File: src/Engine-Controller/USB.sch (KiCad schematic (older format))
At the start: 1 part, among them P2 USB

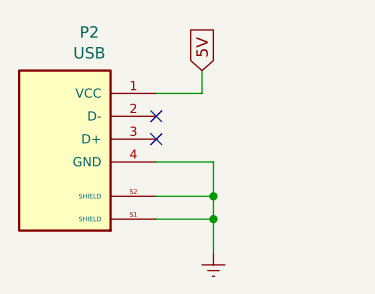
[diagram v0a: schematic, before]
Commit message: Wired 5V power multiplexor
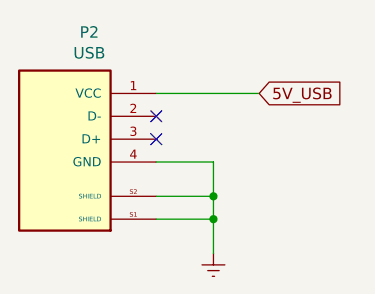
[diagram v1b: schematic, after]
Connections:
- net 5V renamed 5V_USB
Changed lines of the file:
@@
 Wire Wire Line
 	5950 4450 5950 4600
-Wire Wire Line
-	5700 3900 5900 3900
-Wire Wire Line
-	5900 3900 5900 3800
 $Comp
 L Engine-Controller:USB P2
@@
 	-1   0    0    -1
 $EndComp
-Text GLabel 5900 3800 1    50   Input ~ 0
-5V
+Text GLabel 6150 3900 2    50   Input ~ 0
+5V_USB
 NoConn ~ 5700 4000
 NoConn ~ 5700 4100
+Wire Wire Line
+	5700 3900 6150 3900
 $EndSCHEMATC
